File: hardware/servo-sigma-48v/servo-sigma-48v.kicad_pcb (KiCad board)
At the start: 4 copper layers, 64.7 x 71.7 mm, 176 parts, among them J1 CONN_01X02, J2 CONN_02X05, J3 CONN_01X03, J4 CONN_01X03_MALE, J5 CONN_01X05, J6 629_105_150_921, J7 CONN_01X02, Q1 STL160NS3LLH7, Q2 STL160NS3LLH7, Q3 STL160NS3LLH7, Q4 STL160NS3LLH7, Q5 STL160NS3LLH7, Q6 STL160NS3LLH7, Q7 STL160NS3LLH7, Q8 STL160NS3LLH7, U1 ST1S14, U10 OPA4374, U11 L6398, U2 TPS70950, U3 ACS711, U4 L6398, U5 STM32F411RETx, U6 L6398, U7 L6398, U8 TPS70933, U9 OPA4374, Y1 ABM3-8.000MHZ-D2Y-T

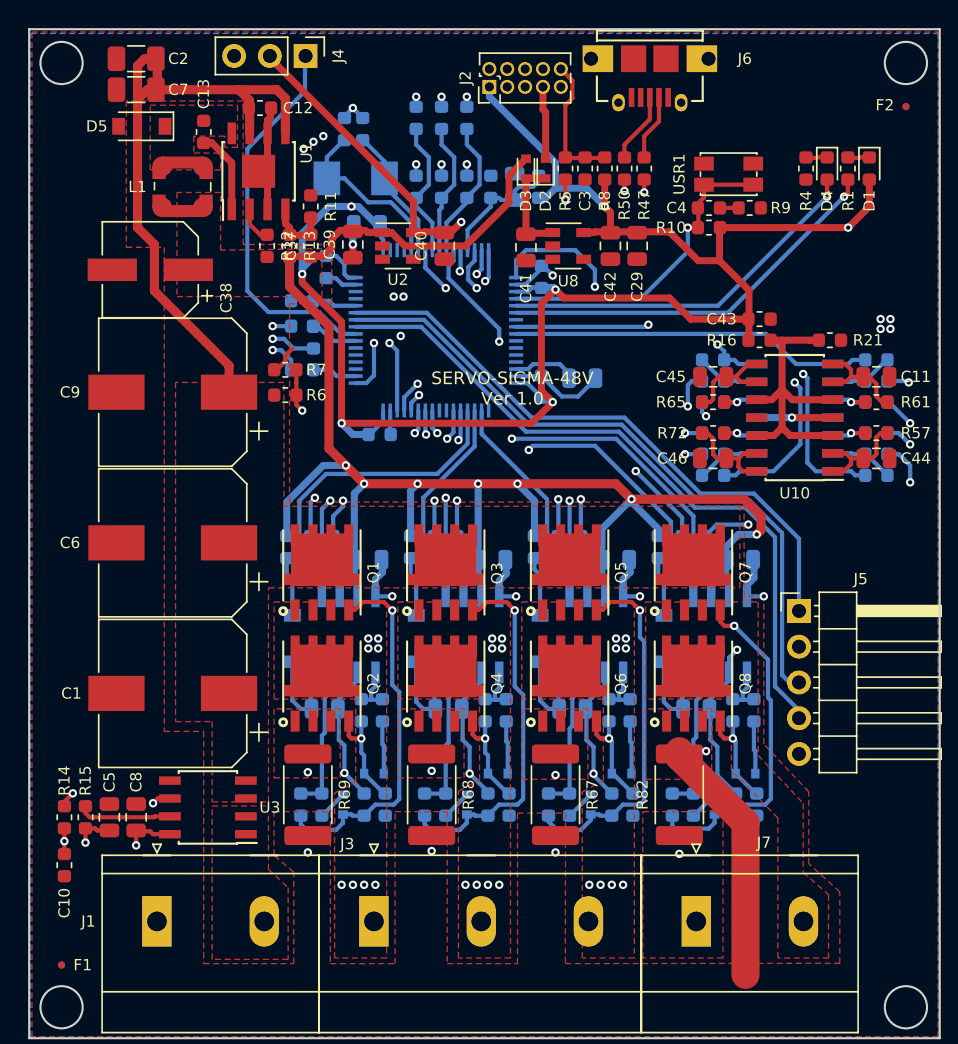
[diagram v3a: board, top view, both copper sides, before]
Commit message: Fixed overlapping footprints
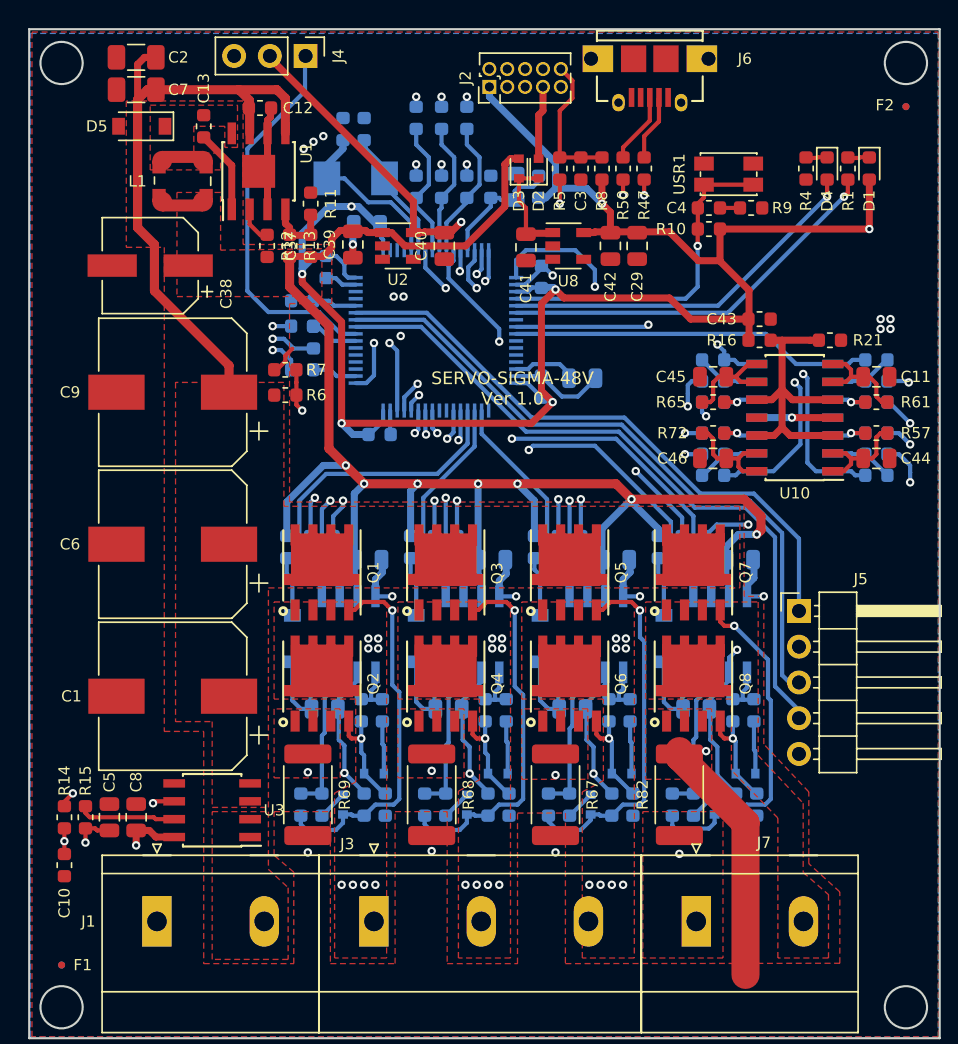
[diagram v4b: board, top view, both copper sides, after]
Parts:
- moved D2 0.50 mm to (118.7, 59.3)
- moved D3 0.50 mm to (117.3, 59.3)
- moved C13 0.40 mm to (94.9, 56.3)
- moved L1 0.40 mm to (93.4, 60.2)
- moved R5 0.40 mm to (120.2, 59.3)
- moved U3 0.36 mm to (95.5, 104.9)
- moved C3 0.30 mm to (121.7, 59.3)
- moved C38 0.30 mm to (91.1, 66.2)
- moved C1 0.20 mm to (92.7, 96.8)
- moved R8 0.20 mm to (123.2, 59.3)
- moved R11 0.20 mm to (102.5, 61.8)
- moved R9 0.10 mm to (133.8, 62.1)
- moved C27 0.10 mm to (104.8, 56.5)
- moved C2 0.10 mm to (90.1, 51.4)
- moved R10 0.10 mm to (130.8, 63.6)
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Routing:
- net +BATT: track 46.7 -> 44.5 mm
- net GND: track 277.2 -> 275.2 mm, vias 37 -> 36
- net /MCU/PA4: track 22.8 -> 24.2 mm
- net +3V3: track 206.3 -> 207.1 mm
